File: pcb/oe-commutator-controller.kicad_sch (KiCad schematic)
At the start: 6 parts

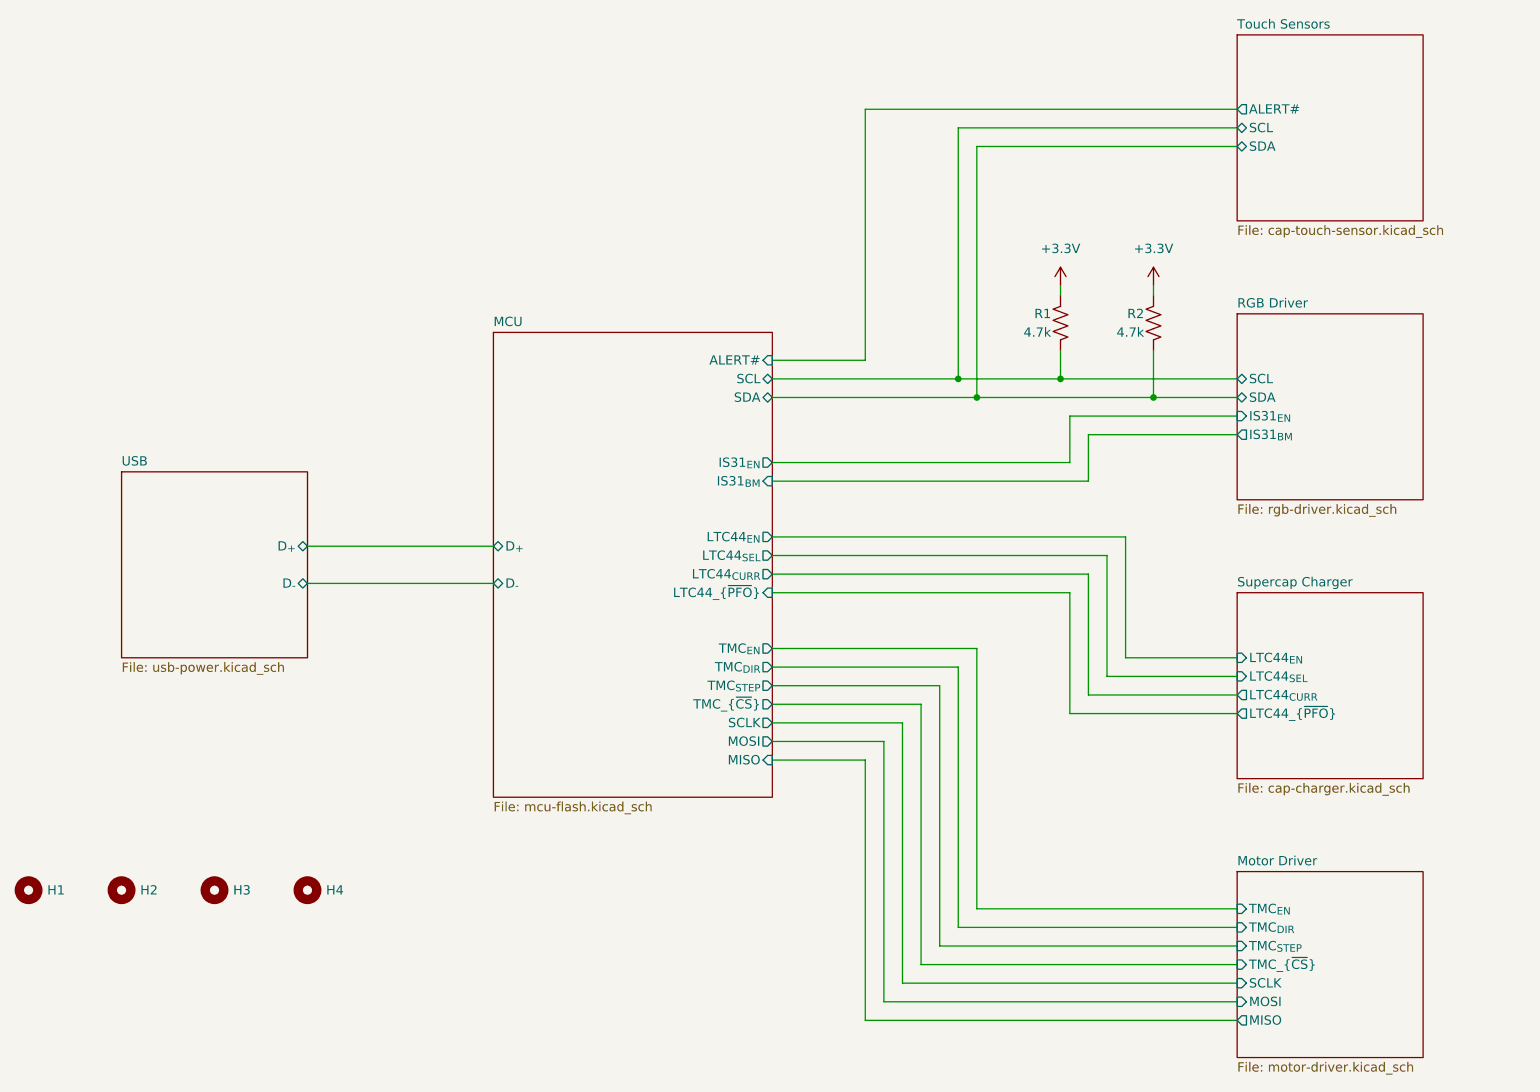
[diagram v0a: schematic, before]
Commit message: Revision E
- Resolve issues 1-11
- Add pdf of rev d schematic for easy comparison
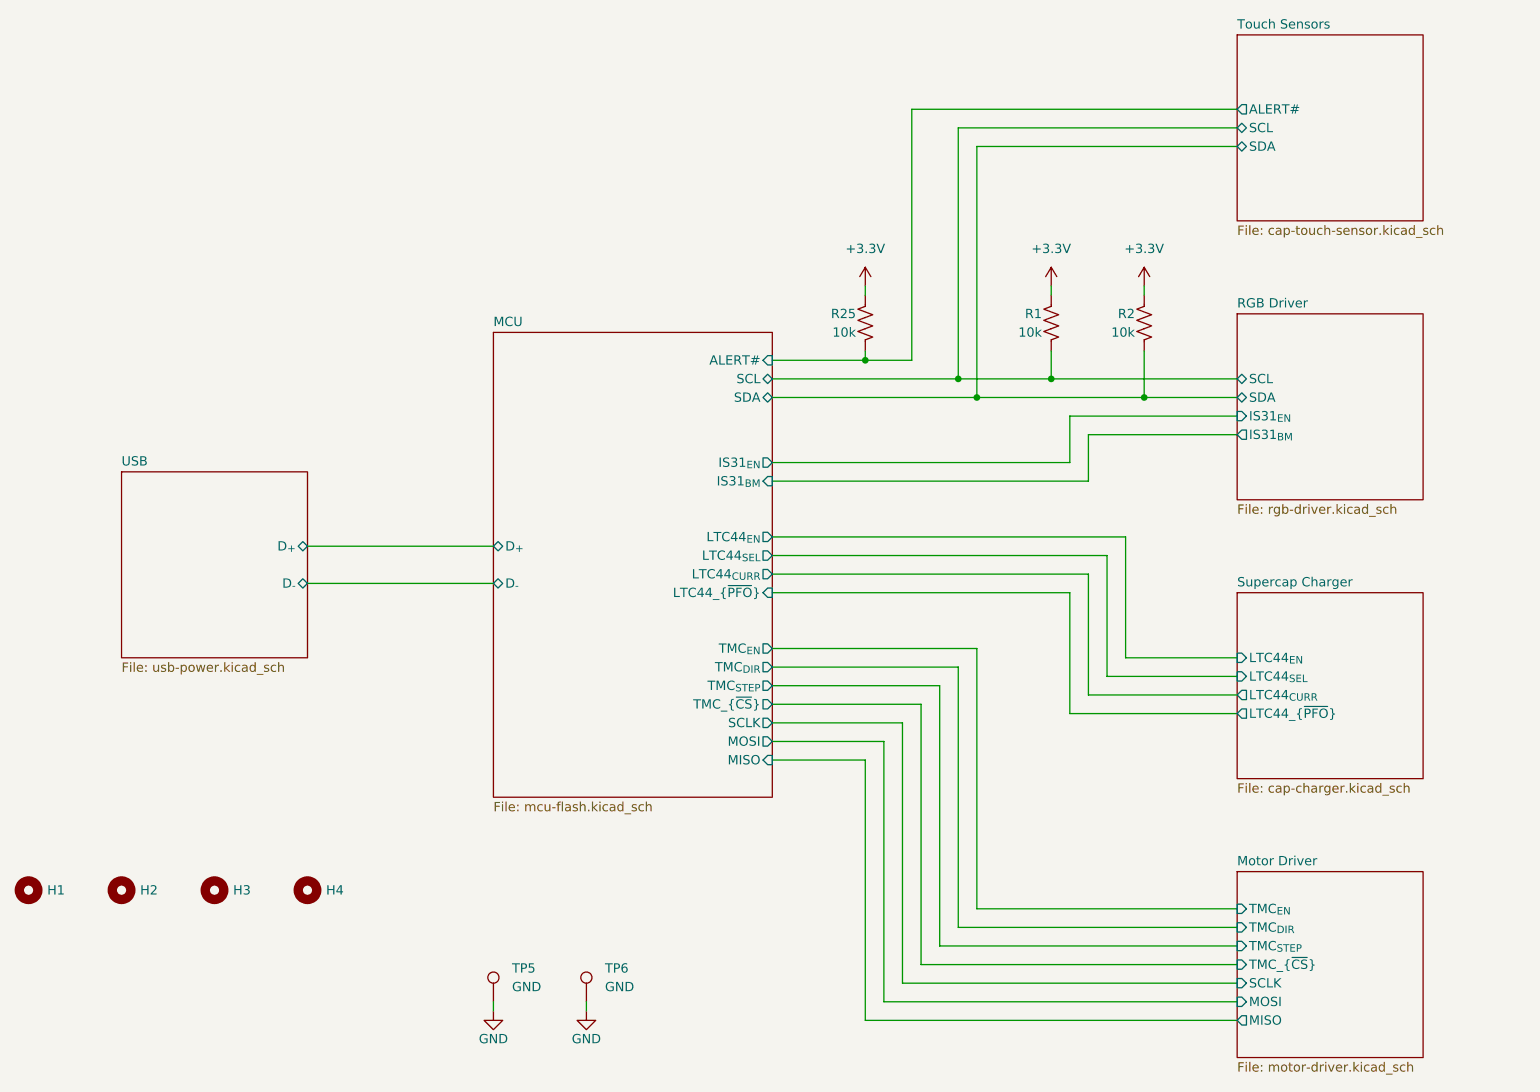
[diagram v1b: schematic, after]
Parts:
- added R25: 10k, Resistor_SMD:R_0603_1608Metric, symbol Device:R_US
- added TP5, TP6: GND, TestPoint:TestPoint_Pad_D2.0mm, symbol Connector:TestPoint
- R1, R2: value 4.7k -> 10k
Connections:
- net +3.3V: now also R25.1
- net MCU/ALERT#: now also R25.2
- new net GND: TP5.1, TP6.1
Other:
- moved on the sheet: R1, R2

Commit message: Address schematic and PCB issues for Rev. E
- Some layout alternations
- Some schematic cleanup
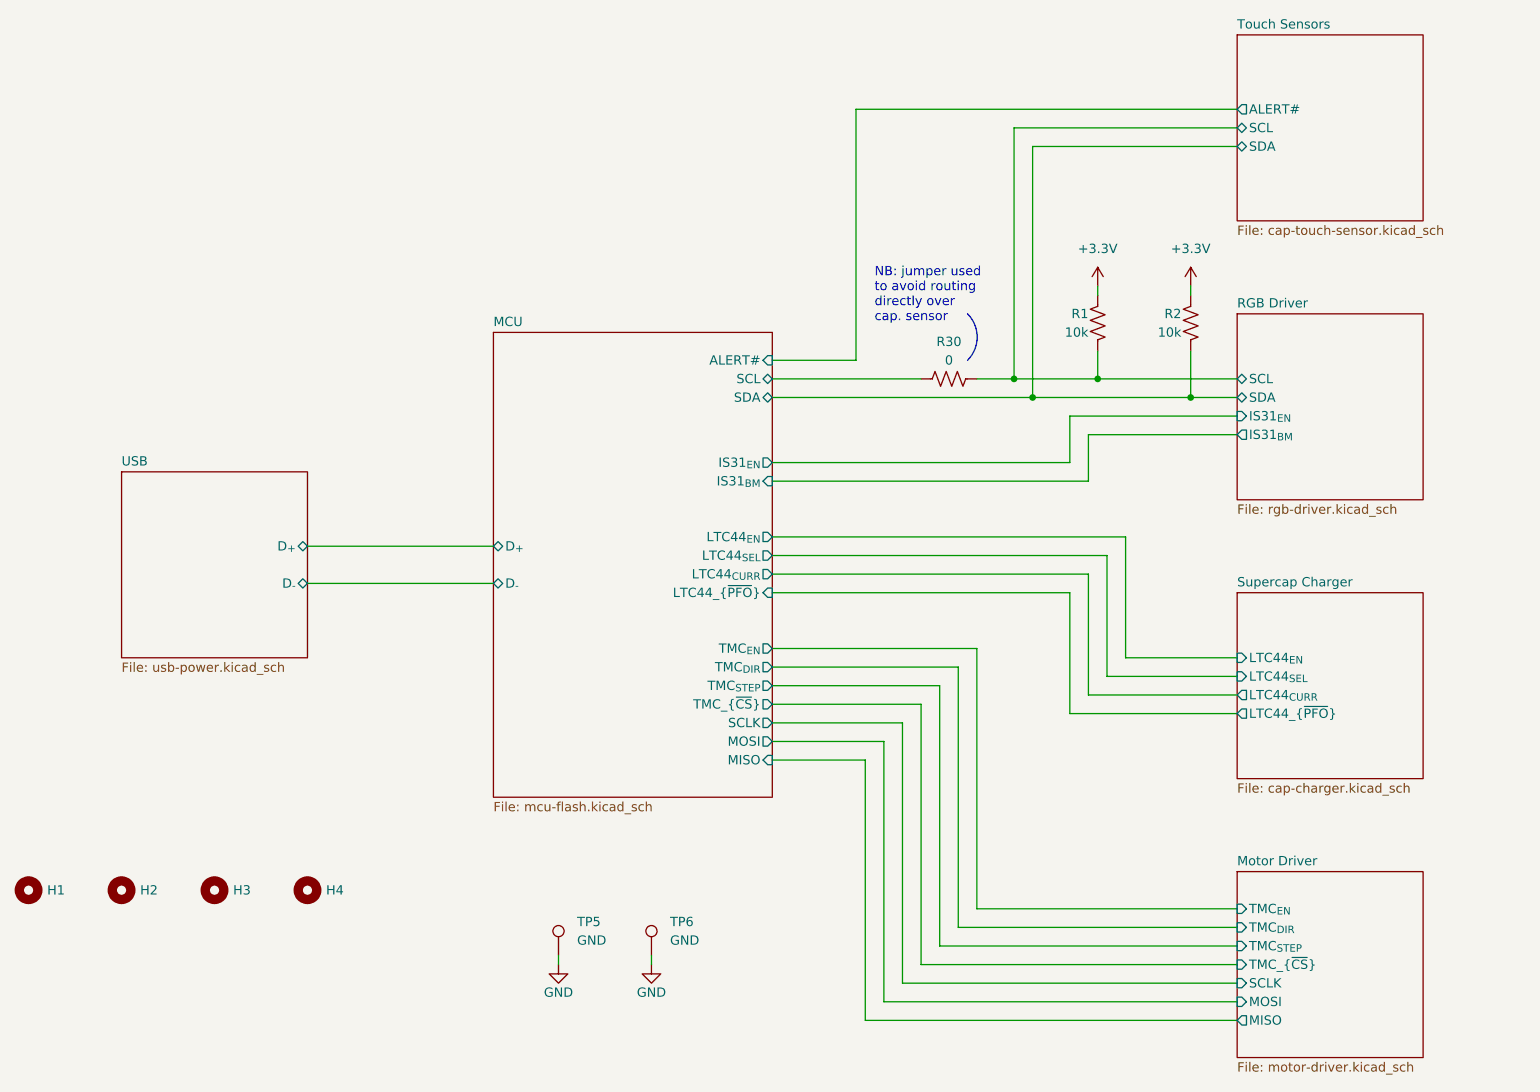
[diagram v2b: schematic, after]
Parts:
- removed R25: 10k, Resistor_SMD:R_0603_1608Metric, symbol Device:R_US
- added R30: 0, Resistor_SMD:R_0603_1608Metric, symbol Device:R_US
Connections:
- net MCU/SCL: now also R30.2; no longer R1.2
- new net RGB Driver/SCL: R1.2, R30.1
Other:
- note added: "NB: jumper used to avoid routing directly over cap. sensor"
- moved on the sheet: R1, R2, TP5, TP6

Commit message: Removed GND plane back layer
- Moved the UART traces a little out of the way of xtal trace
- Labelled debug headers as DNP
- Changed i2c pull-ups back to 4.7k how they were in rev d. I
  changed these by mistake in commit 8da4fdf when reducing BOM component list
- Generated production files - ibom, gerber, drill files
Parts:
- R1, R2: value 10k -> 4.7k
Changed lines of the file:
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@@
 			)
 		)
-		(property "Value" "10k"
+		(property "Value" "4.7k"
 			(at 182.88 59.69 0)
 			(effects
@@
 			)
 		)
-		(property "Value" "10k"
+		(property "Value" "4.7k"
 			(at 195.58 59.69 0)
 			(effects

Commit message: Some edits during PR review
- Silkscreen moved on board
- Get rid of value text in fab layer
- Invert TMC_EN name to indicate correct logic
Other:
- sheet MCU ports: added TMC_{~{EN}}; removed TMC_{EN}
- sheet Motor Driver ports: added TMC_{~{EN}}; removed TMC_{EN}
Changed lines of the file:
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@@
 			)
 		)
-		(pin "TMC_{EN}" input
+		(pin "TMC_{~{EN}}" input
 			(at 203.2 138.43 180)
 			(effects
@@
 			)
 		)
-		(pin "TMC_{EN}" output
+		(pin "TMC_{~{EN}}" output
 			(at 139.7 102.87 0)
 			(effects

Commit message: Revision G edits
- Move R10 & R13 silk screen designators closer to their respective
  resistors
- Add specific part numbers to C15 & C15 which are xtal caps w/ NP0 temp
  coefficient
- Update libraries to remove solder paste from big caps' footprint
- Made boot select button footprint to datasheet spec (had to move some
  traces to do this)
- Remove solder paste from LED footprint
- Update revision f-->g in sch, pcb, & pcb's silk screen
- No solder paste in the LED footprint
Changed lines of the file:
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@@
 	(title_block
 		(title "Open Ephys Commutator Controller")
-		(rev "F")
+		(rev "G")
 		(company "Open Ephys, Inc.")
 		(comment 1 "Cris Sharp")
@@
 			)
 		)
-		(pin "LTC44_{CURR}" output
-			(at 139.7 92.71 0)
-			(effects
-				(font
-					(size 1.27 1.27)
-				)
-				(justify right)
-			)
-		)
 		(pin "LTC44_{~{PFO}}" input
 			(at 139.7 95.25 0)
@@
 			(effects
 				(font
+					(size 1.27 1.27)
+				)
+				(justify right)
+			)
+		)
+		(pin "LTC44_{CURR}" input
+			(at 139.7 92.71 0)
+			(effects
+				(font
